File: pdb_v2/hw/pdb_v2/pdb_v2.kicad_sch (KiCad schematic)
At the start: 78 parts, among them J1 XT30-M_Ver, J2 JST-PH_01x02, J3 JST-PH_01x02, J4 JST-PH_01x02, J5 JST-PH_01x02, Q1 60Vds, U1 LMR51635XFDDCR, U2 AP63205WU-7, U3 AP63203WU-7

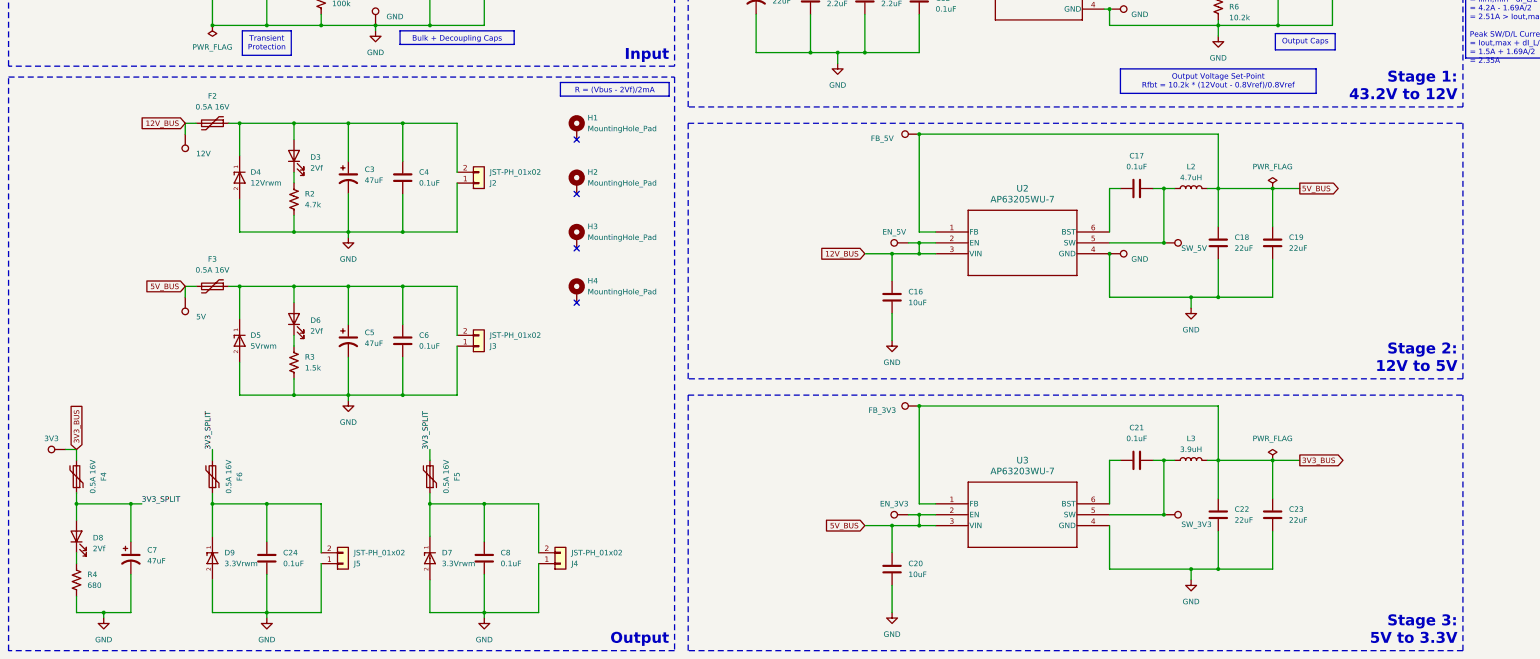
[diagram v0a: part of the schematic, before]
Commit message: Removed 12V to 5V stage
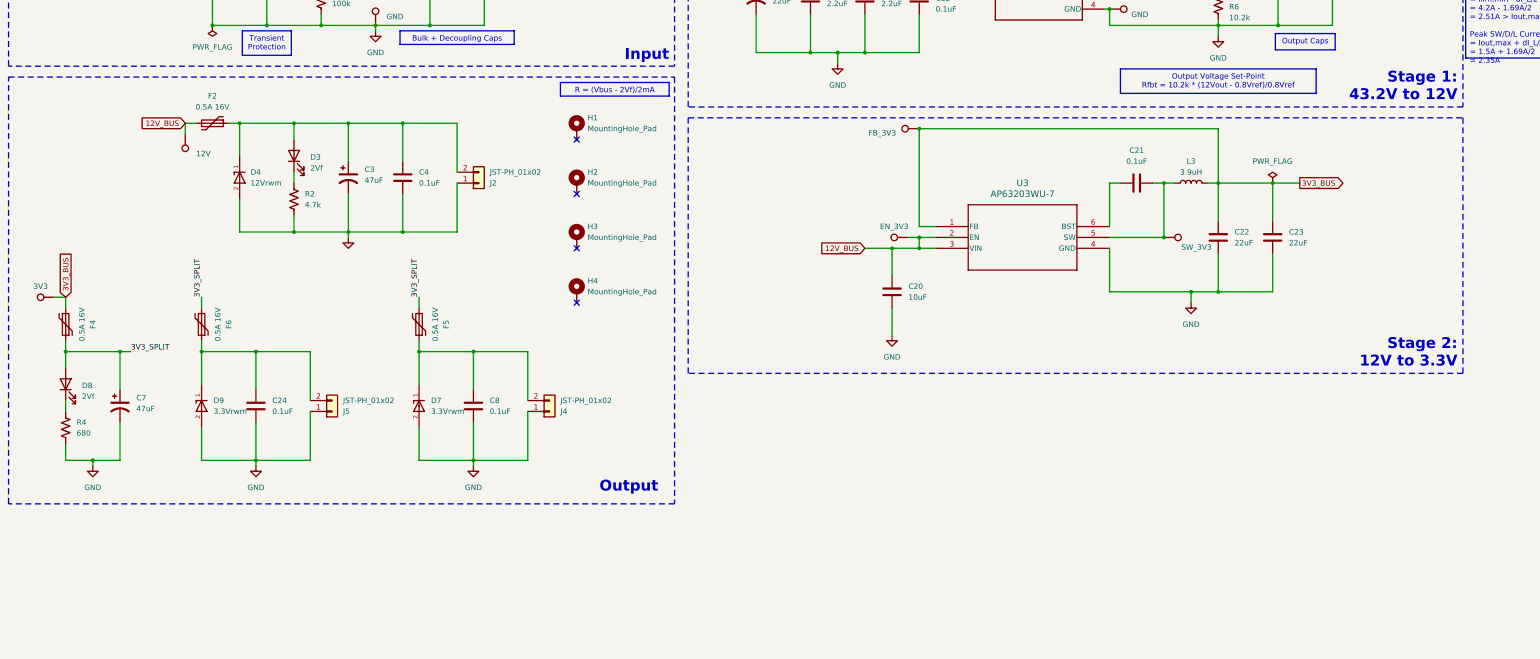
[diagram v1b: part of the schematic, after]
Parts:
- removed 5V1: 5V, test_point_custom:TestPoint_Pad_D1.0mm, symbol Connector:TestPoint
- removed C16: 10uF, Capacitor_SMD:C_1206_3216Metric_Pad1.33x1.80mm_HandSolder, symbol Device:C
- removed C17, C6: 0.1uF, Capacitor_SMD:C_0603_1608Metric_Pad1.08x0.95mm_HandSolder, symbol Device:C
- removed C18, C19: 22uF, Capacitor_SMD:C_1210_3225Metric_Pad1.33x2.70mm_HandSolder, symbol Device:C
- removed C5: 47uF, Capacitor_SMD:CP_Elec_6.3x7.7, symbol Device:C_Polarized_US
- removed D5: 5Vrwm, ESD5Z5.0T1G:SOD-523_0P9X1P3_ONS, symbol SMBJ51A-13-F:SMBJ51A-13-F
- removed D6: 2Vf, LED_SMD:LED_0805_2012Metric_Pad1.15x1.40mm_HandSolder, symbol Device:LED
- removed EN_5V1: EN_5V, test_point_custom:TestPoint_Pad_D1.0mm, symbol Connector:TestPoint
- removed F3: 0.5A 16V, 0ZCH0050FF2G:0ZCH_BEL, symbol Device:Polyfuse
- removed FB_5V1: FB_5V, test_point_custom:TestPoint_Pad_D1.0mm, symbol Connector:TestPoint
- removed GND3: GND, test_point_custom:TestPoint_Pad_D1.0mm, symbol Connector:TestPoint
- removed J3: JST-PH_01x02, Connector_JST:JST_PH_S2B-PH-K_1x02_P2.00mm_Horizontal, symbol Connector_Generic:Conn_01x02
- removed L2: 4.7uH, 7447779004:IND_7345R_WE-PD_WRE, symbol Device:L
- removed R3: 1.5k, Resistor_SMD:R_0603_1608Metric_Pad0.98x0.95mm_HandSolder, symbol Device:R_US
- removed SW_5V1: SW_5V, test_point_custom:TestPoint_Pad_D1.0mm, symbol Connector:TestPoint
- removed U2: AP63205WU-7, AP63205WU-7:SOIC_05WU-7_DIO, symbol AP63205WU-7:AP63205WU-7
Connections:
- net 5V_BUS is gone; now on net 12V_BUS: C20.1, EN_3V3.1, U3.2 (EN), U3.3 (VIN)
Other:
- note added: "Stage 2: 12V to 3.3V"
- note removed: "Stage 2: 12V to 5V"
- note removed: "Stage 3: 5V to 3.3V"
- moved on the sheet: C20, C21, C22, C23, C24, C7, C8, D7, D8, D9, F4, F5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

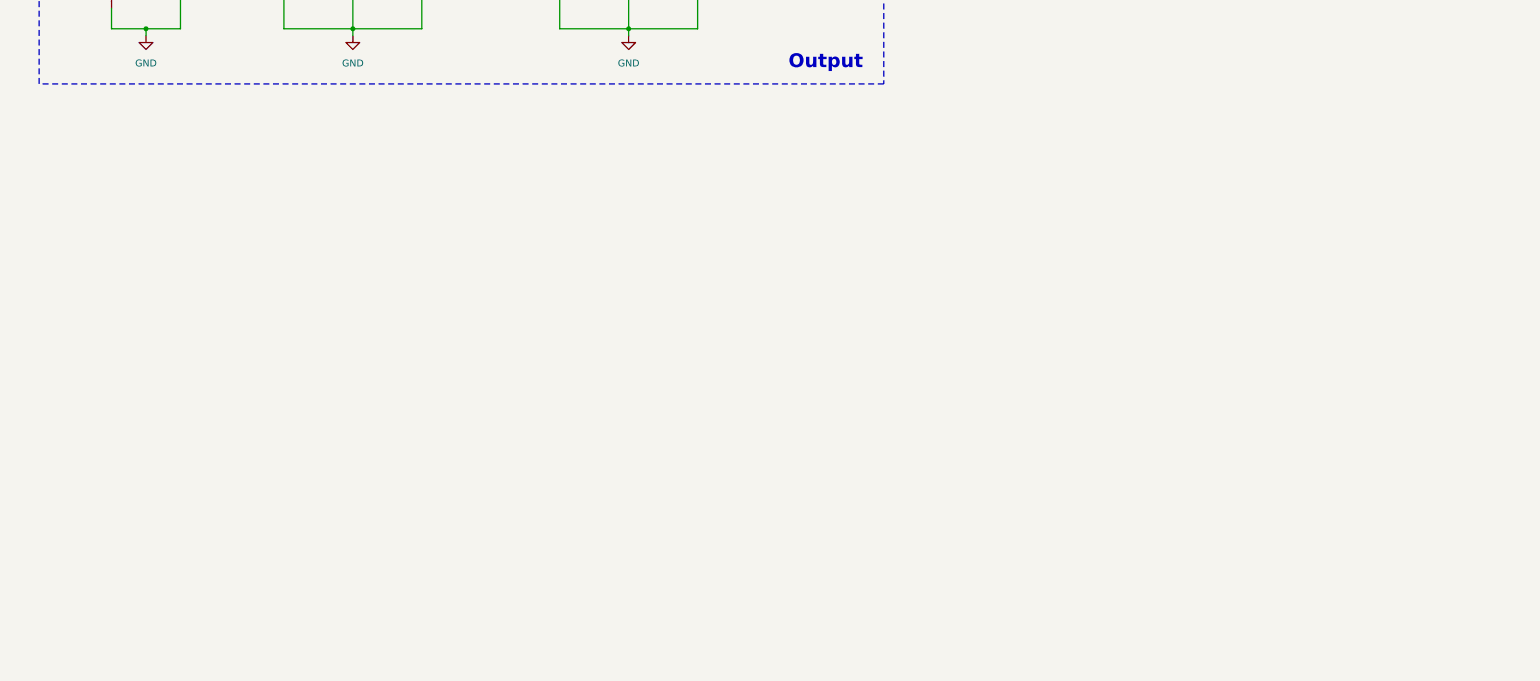
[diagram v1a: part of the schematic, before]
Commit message: Added telemetry components
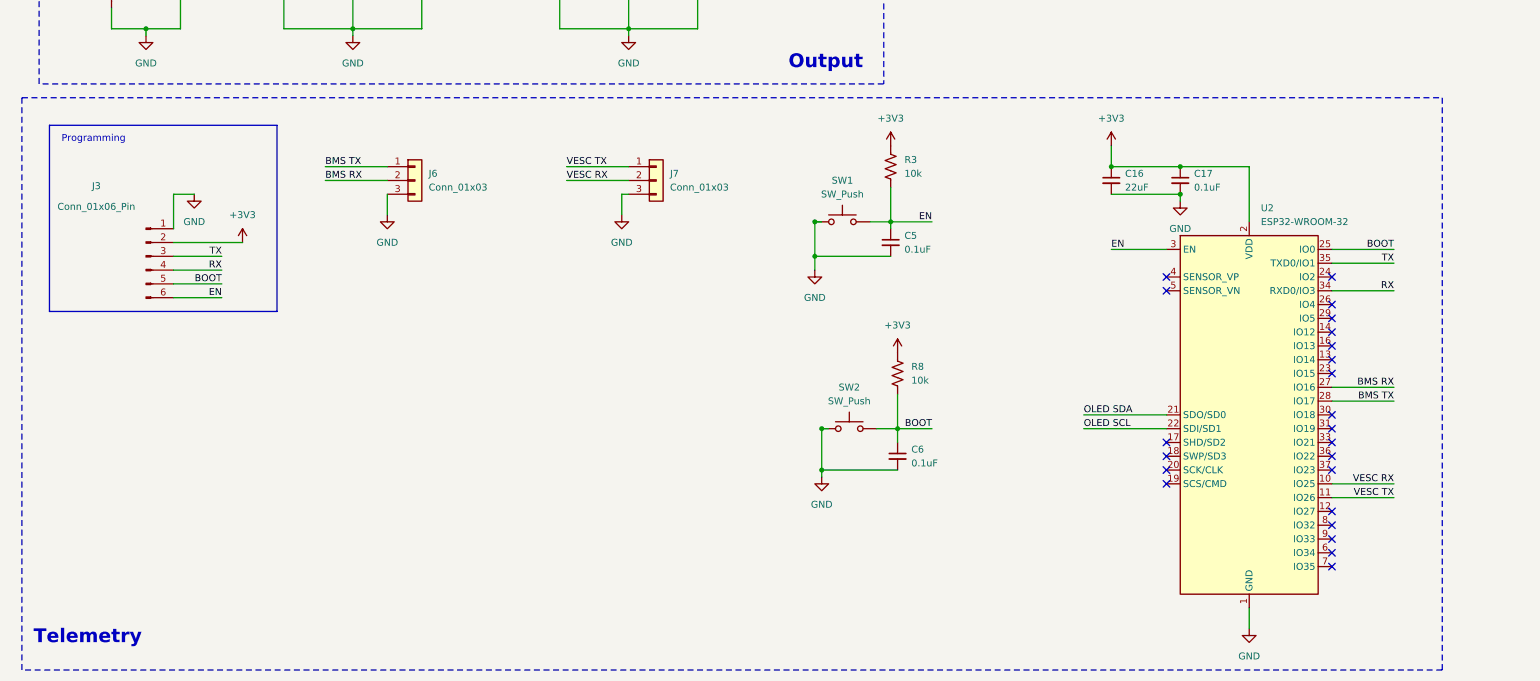
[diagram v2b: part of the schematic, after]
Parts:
- added C16: 22uF, symbol Device:C_Small
- added C17, C5, C6: 0.1uF, symbol Device:C_Small
- added J3: Conn_01x06_Pin, symbol Connector:Conn_01x06_Pin
- added J6, J7: Conn_01x03, symbol Connector_Generic:Conn_01x03
- added R3, R8: 10k, Resistor_SMD:R_0805_2012Metric, symbol Device:R_US
- added SW1, SW2: SW_Push, symbol Switch:SW_Push
- added U2: ESP32-WROOM-32, RF_Module:ESP32-WROOM-32, symbol RF_Module:ESP32-WROOM-32
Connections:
- net GND: now also C16.2, C17.2, C5.2, C6.2, J3.1 (Pin_1), J6.3 (Pin_3), J7.3 (Pin_3), SW1.1, SW2.1, U2.1 (GND), U2.15 (GND), U2.38 (GND), U2.39 (GND)
- new net +3V3: C16.1, C17.1, J3.2 (Pin_2), R3.1, R8.1, U2.2 (VDD)
- new net BMS RX: J6.2 (Pin_2), U2.27 (IO16)
- new net BMS TX: J6.1 (Pin_1), U2.28 (IO17)
- new net BOOT: C6.1, J3.5 (Pin_5), R8.2, SW2.2, U2.25 (IO0)
- new net EN: C5.1, J3.6 (Pin_6), R3.2, SW1.2, U2.3 (EN)
- new net OLED SCL: U2.22 (SDI/SD1)
- new net OLED SDA: U2.21 (SDO/SD0)
- new net RX: J3.4 (Pin_4), U2.34 (RXD0/IO3)
- new net TX: J3.3 (Pin_3), U2.35 (TXD0/IO1)
- new net VESC RX: J7.2 (Pin_2), U2.10 (IO25)
- new net VESC TX: J7.1 (Pin_1), U2.11 (IO26)
- no-connect marks 4 -> 27
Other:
- note added: "Programming"
- note added: "Telemetry"

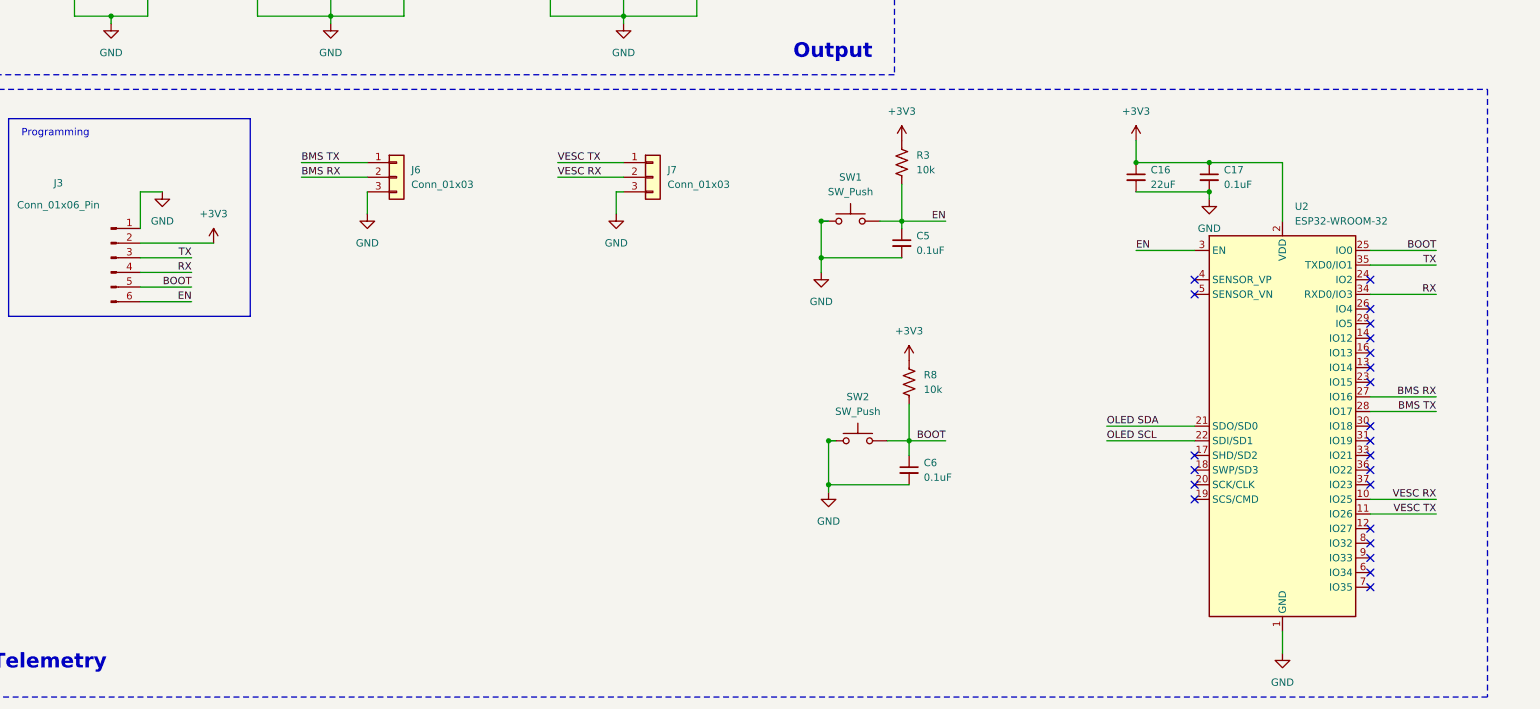
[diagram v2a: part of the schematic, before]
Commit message: Added footprints
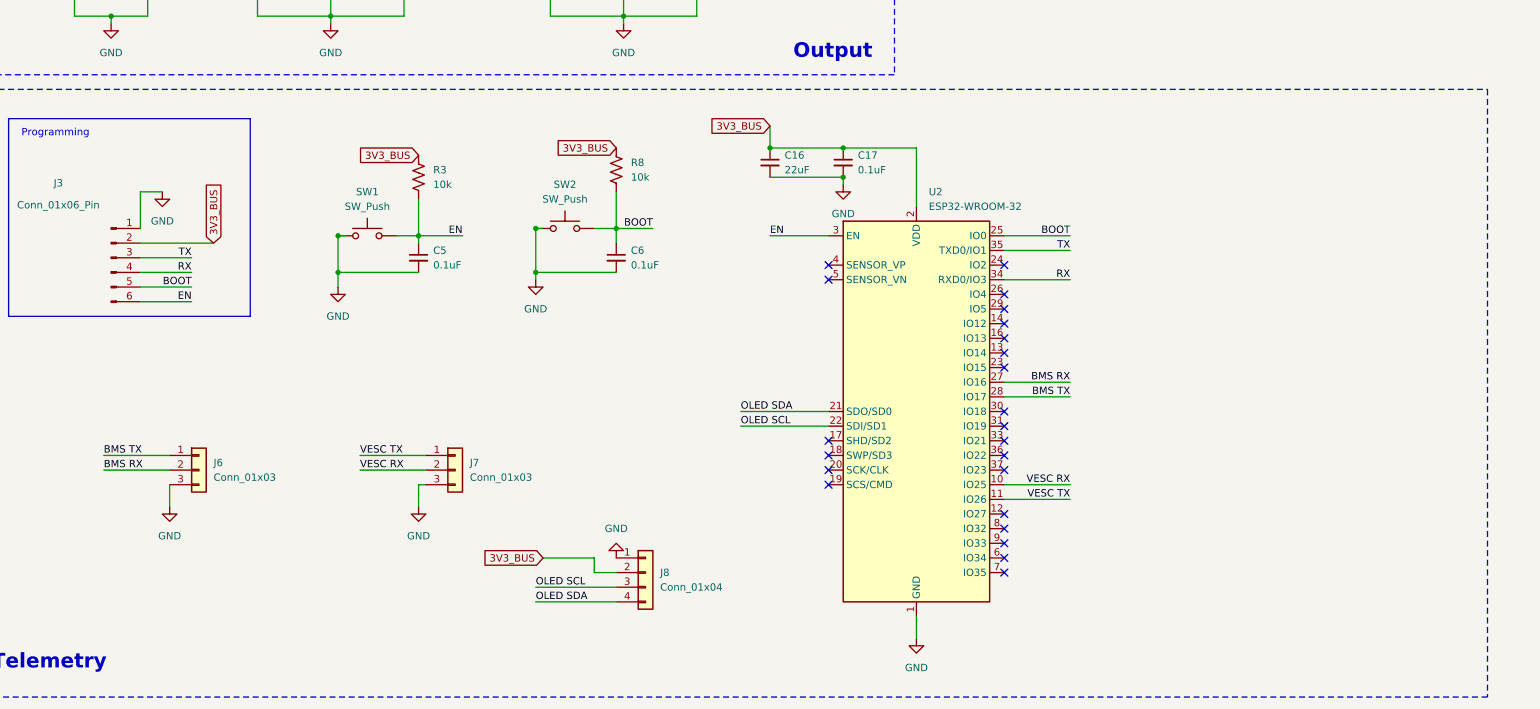
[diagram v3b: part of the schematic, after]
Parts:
- added J8: Conn_01x04, Connector_PinHeader_2.54mm:PinHeader_1x04_P2.54mm_Vertical, symbol Connector_Generic:Conn_01x04
- C16: footprint (none) -> Capacitor_SMD:C_1210_3225Metric_Pad1.33x2.70mm_HandSolder
- C17, C5, C6: footprint (none) -> Capacitor_SMD:C_0603_1608Metric_Pad1.08x0.95mm_HandSolder
- J3: footprint (none) -> Connector_PinHeader_2.54mm:PinHeader_1x06_P2.54mm_Vertical
- R3, R8: footprint Resistor_SMD:R_0805_2012Metric -> Resistor_SMD:R_0603_1608Metric_Pad0.98x0.95mm_HandSolder
- SW1, SW2: footprint (none) -> Button_Switch_SMD:SW_SPST_TL3342
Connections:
- net +3V3 is gone; now on net 3V3_BUS: C16.1, C17.1, J3.2 (Pin_2), R3.1, R8.1, U2.2 (VDD)
- net 3V3_BUS: now also J8.2 (Pin_2)
- net GND: now also J8.1 (Pin_1)
- net OLED SCL: now also J8.3 (Pin_3)
- net OLED SDA: now also J8.4 (Pin_4)
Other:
- moved on the sheet: C16, C17, C5, C6, J6, J7, R3, R8, SW1, SW2, U2

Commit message: added footprints for connectors
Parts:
- J6, J7: footprint (none) -> Connector_JST:JST_PH_B3B-PH-K_1x03_P2.00mm_Vertical
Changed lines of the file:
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@@
 			)
 		)
-		(property "Footprint" ""
+		(property "Footprint" "Connector_JST:JST_PH_B3B-PH-K_1x03_P2.00mm_Vertical"
 			(at 57.15 243.84 0)
 			(effects
@@
 			)
 		)
-		(property "Footprint" ""
+		(property "Footprint" "Connector_JST:JST_PH_B3B-PH-K_1x03_P2.00mm_Vertical"
 			(at 101.6 243.84 0)
 			(effects

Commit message: cleaned up, added oled footprint, arranged some components
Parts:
- J8: footprint Connector_PinHeader_2.54mm:PinHeader_1x04_P2.54mm_Vertical -> SSD1306:128x64OLED
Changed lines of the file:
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@@
 			)
 		)
-		(property "Footprint" "Connector_PinHeader_2.54mm:PinHeader_1x04_P2.54mm_Vertical"
+		(property "Footprint" "SSD1306:128x64OLED"
 			(at 134.62 261.62 0)
 			(effects

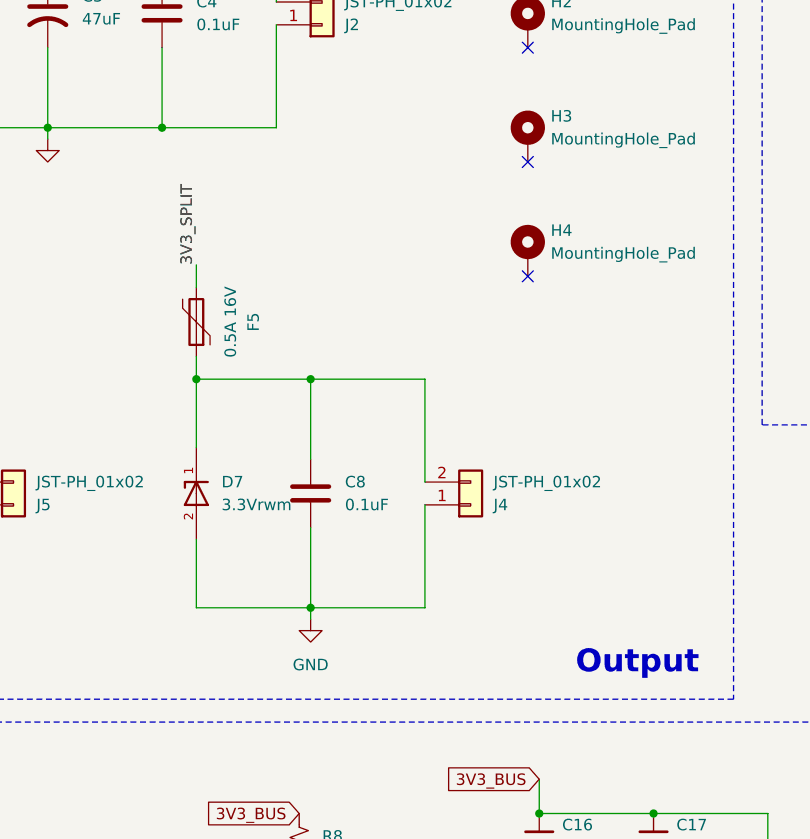
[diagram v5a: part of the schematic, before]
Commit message: removed second 3v3 connector, arranged telemetry components
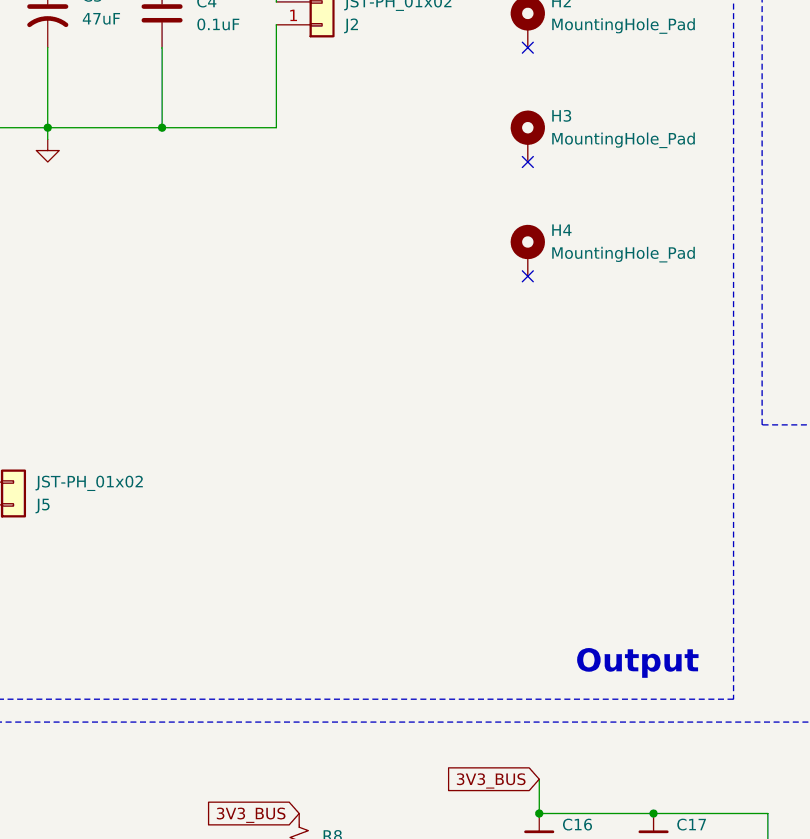
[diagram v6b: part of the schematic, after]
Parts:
- removed C8: 0.1uF, Capacitor_SMD:C_0603_1608Metric_Pad1.08x0.95mm_HandSolder, symbol Device:C
- removed D7: 3.3Vrwm, ESD5Z5.0T1G:SOD-523_0P9X1P3_ONS, symbol SMBJ51A-13-F:SMBJ51A-13-F
- removed F5: 0.5A 16V, 0ZCH0050FF2G:0ZCH_BEL, symbol Device:Polyfuse
- removed J4: JST-PH_01x02, Connector_JST:JST_PH_S2B-PH-K_1x02_P2.00mm_Horizontal, symbol Connector_Generic:Conn_01x02

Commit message: fixed drc errors
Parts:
- J2, J5: footprint Connector_JST:JST_PH_S2B-PH-K_1x02_P2.00mm_Horizontal -> Connector_JST:JST_PH_B2B-PH-K_1x02_P2.00mm_Vertical
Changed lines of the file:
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@@
 			)
 		)
-		(property "Footprint" "Connector_JST:JST_PH_S2B-PH-K_1x02_P2.00mm_Horizontal"
+		(property "Footprint" "Connector_JST:JST_PH_B2B-PH-K_1x02_P2.00mm_Vertical"
 			(at 132.08 100.33 0)
 			(effects
@@
 			)
 		)
-		(property "Footprint" "Connector_JST:JST_PH_S2B-PH-K_1x02_P2.00mm_Horizontal"
+		(property "Footprint" "Connector_JST:JST_PH_B2B-PH-K_1x02_P2.00mm_Vertical"
 			(at 97.79 153.67 0)
 			(effects

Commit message: added 2 leds on esp32, moved components
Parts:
- added D5, D6: LED, LED_SMD:LED_0603_1608Metric_Pad1.05x0.95mm_HandSolder, symbol Device:LED
- added R10, R9: 1k, Resistor_SMD:R_0603_1608Metric_Pad0.98x0.95mm_HandSolder, symbol Device:R_US
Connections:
- net 3V3_BUS: now also R9.1
- net GND: now also D5.1 (K), D6.1 (K)
- net at U2.31 (IO19): now also R10.1
- new net: D5.2 (A), R9.2
- new net: D6.2 (A), R10.2
- no-connect marks 27 -> 26
